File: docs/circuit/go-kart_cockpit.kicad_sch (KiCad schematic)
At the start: 41 parts, among them P1 Power, Q1 TIP120, SW1 SW_MEC_5E, X1 Taster rechts (male), X10 Bluetooth-Modul, X11 Display (male), X12 PD7, X13 SDA, X14 PG4, X15 AVR-ISP-10, X16 Taster links (male), X17 Start/Stop/Rückwärts, X2 5V, X3 GND, X4 24V Hupe, X5 SCL, X6 CS, X7 PB6, X8 J5, X9 J3

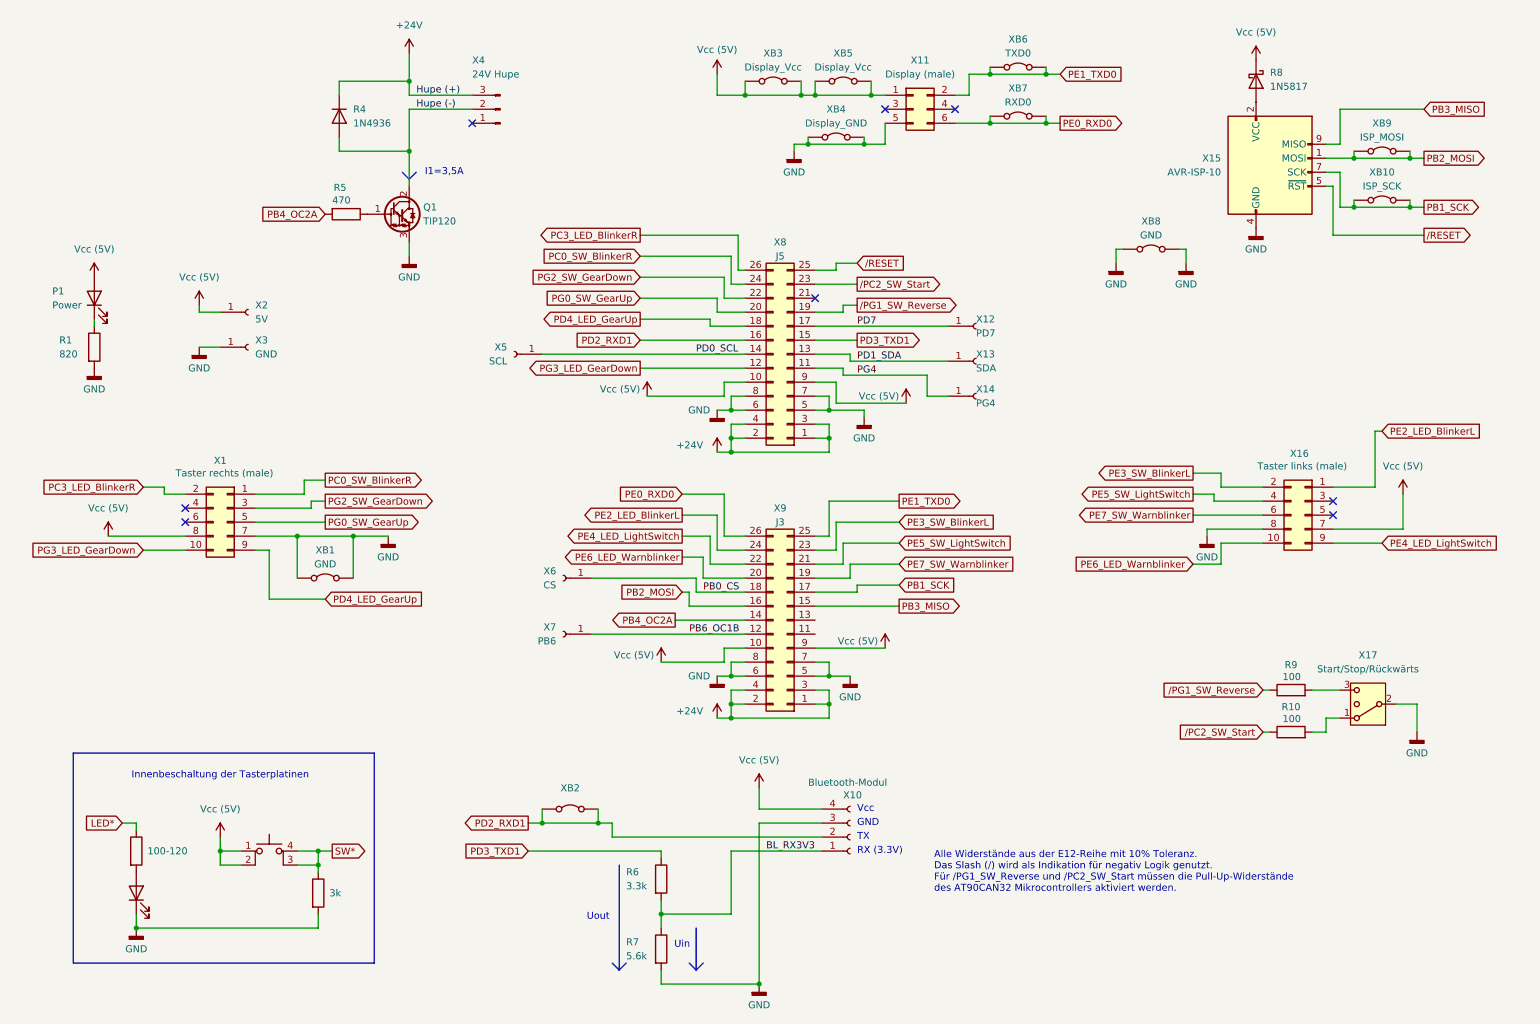
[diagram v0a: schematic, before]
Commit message: feat(PCB): add pull down resistor in preperation for FET
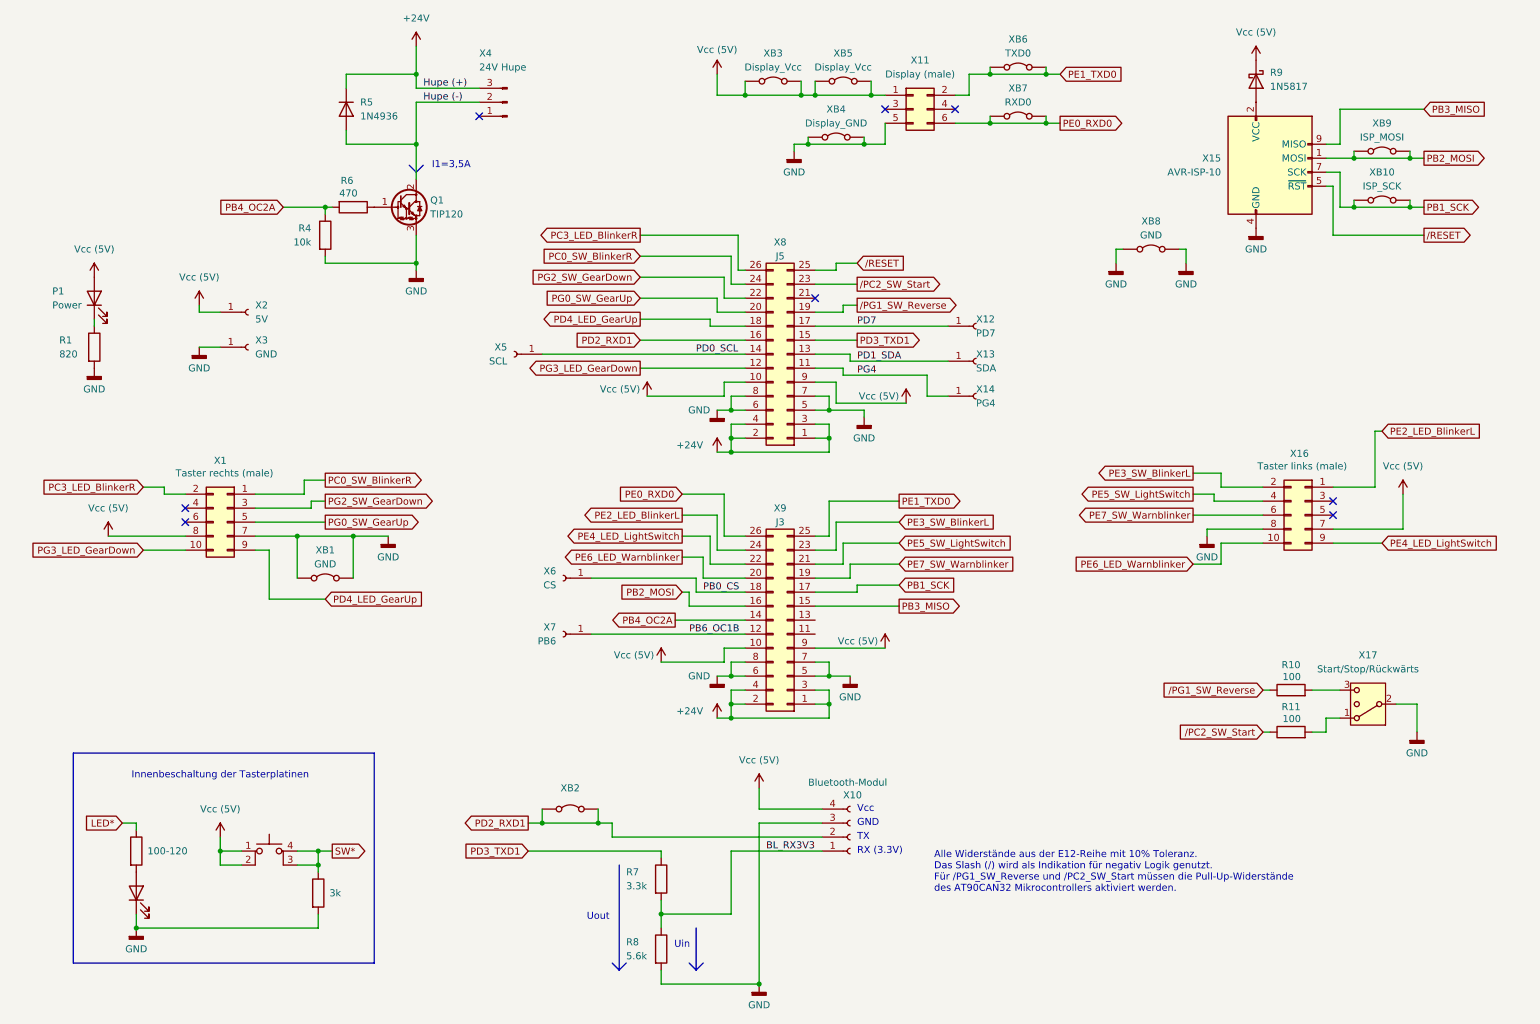
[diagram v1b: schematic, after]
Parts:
- added R4: 10k, Resistor_THT:R_Axial_DIN0207_L6.3mm_D2.5mm_P7.62mm_Horizontal, symbol Device:R
- renumbered R9 to R10, R10 to R11, R4 to R5, R5 to R6, R6 to R7, R7 to R8, R8 to R9
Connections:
- net GND: now also R4.2
- net PB4_OC2A: now also R4.1
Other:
- moved on the sheet: Q1, R5, R6, X4

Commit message: feat(PCB): improve connectors and position
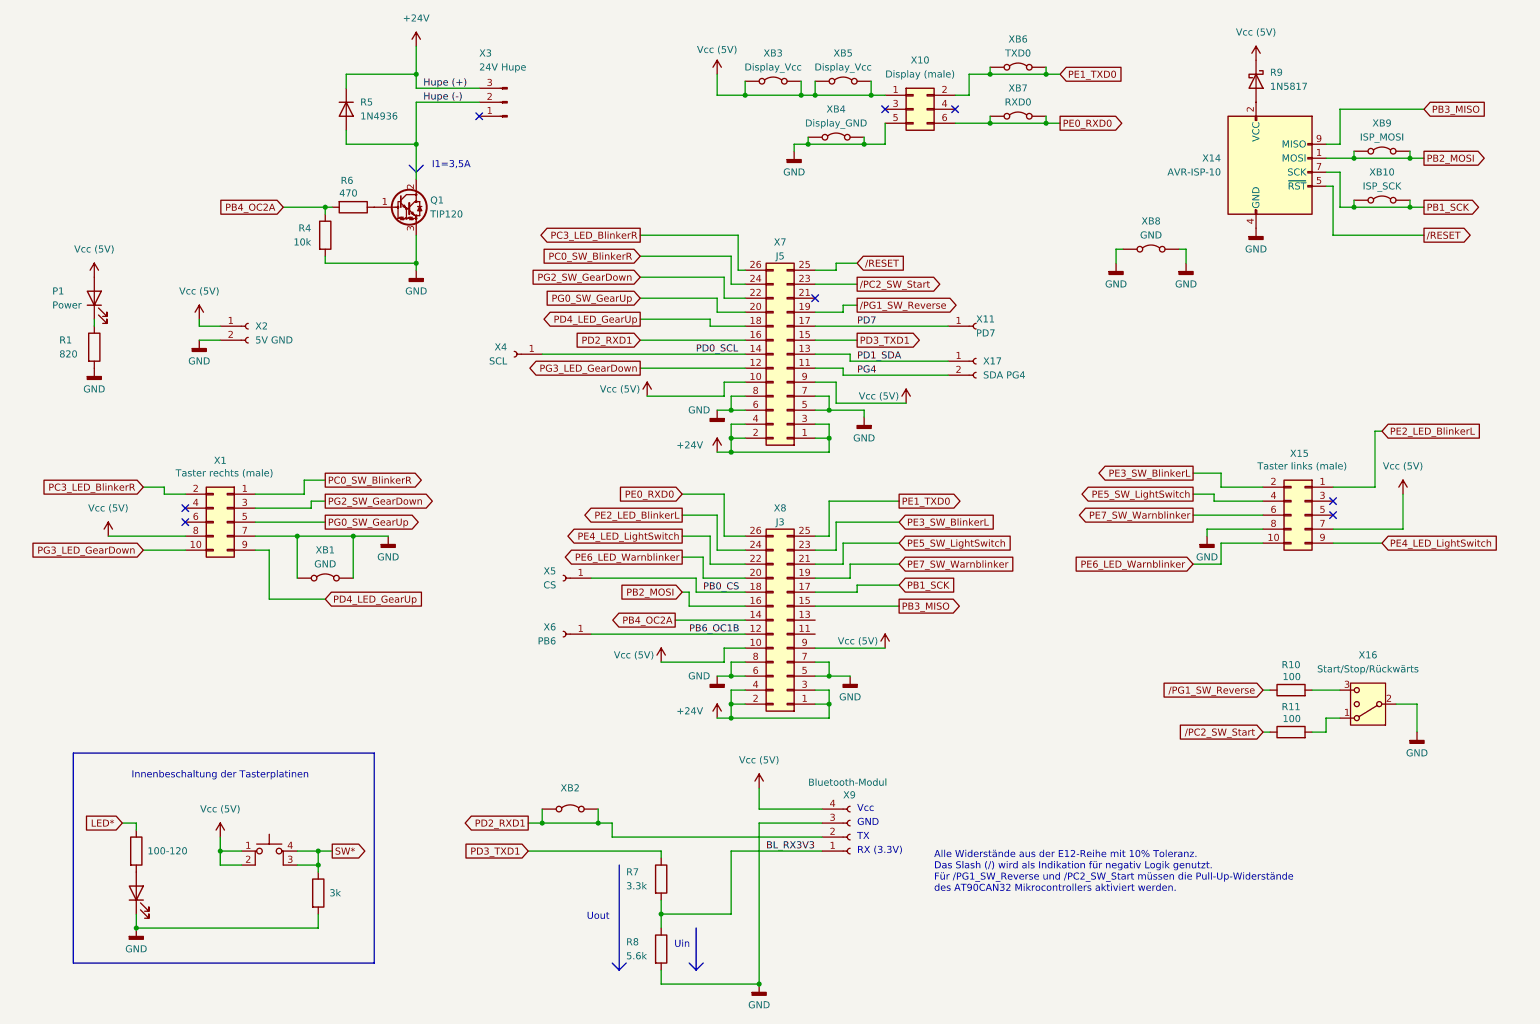
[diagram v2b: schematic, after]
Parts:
- removed X13: SDA, Connector_PinSocket_2.54mm:PinSocket_1x01_P2.54mm_Vertical, symbol Connector:Conn_01x01_Socket
- removed X14: PG4, Connector_PinSocket_2.54mm:PinSocket_1x01_P2.54mm_Vertical, symbol Connector:Conn_01x01_Socket
- removed X2: 5V, Connector_PinSocket_2.54mm:PinSocket_1x01_P2.54mm_Vertical, symbol Connector:Conn_01x01_Socket
- removed X3: GND, Connector_PinSocket_2.54mm:PinSocket_1x01_P2.54mm_Vertical, symbol Connector:Conn_01x01_Socket
- added X17: SDA PG4, Connector_PinSocket_2.54mm:PinSocket_1x02_P2.54mm_Vertical, symbol Connector:Conn_01x02_Socket
- added X2: 5V GND, Connector_PinSocket_2.54mm:PinSocket_1x02_P2.54mm_Vertical, symbol Connector:Conn_01x02_Socket
- renumbered X11 to X10, X12 to X11, X15 to X14, X16 to X15, X17 to X16, X4 to X3, X5 to X4, X6 to X5, X7 to X6, X8 to X7, X9 to X8, X10 to X9
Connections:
- net GND: now also X2.2 (Pin_2)
- net PD1_SDA: now also X17.1 (Pin_1)
- net PG4: now also X17.2 (Pin_2)
- net Vcc (5V): now also X2.1 (Pin_1)

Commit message: feat(PCB): replace TIP120 with MOSFET
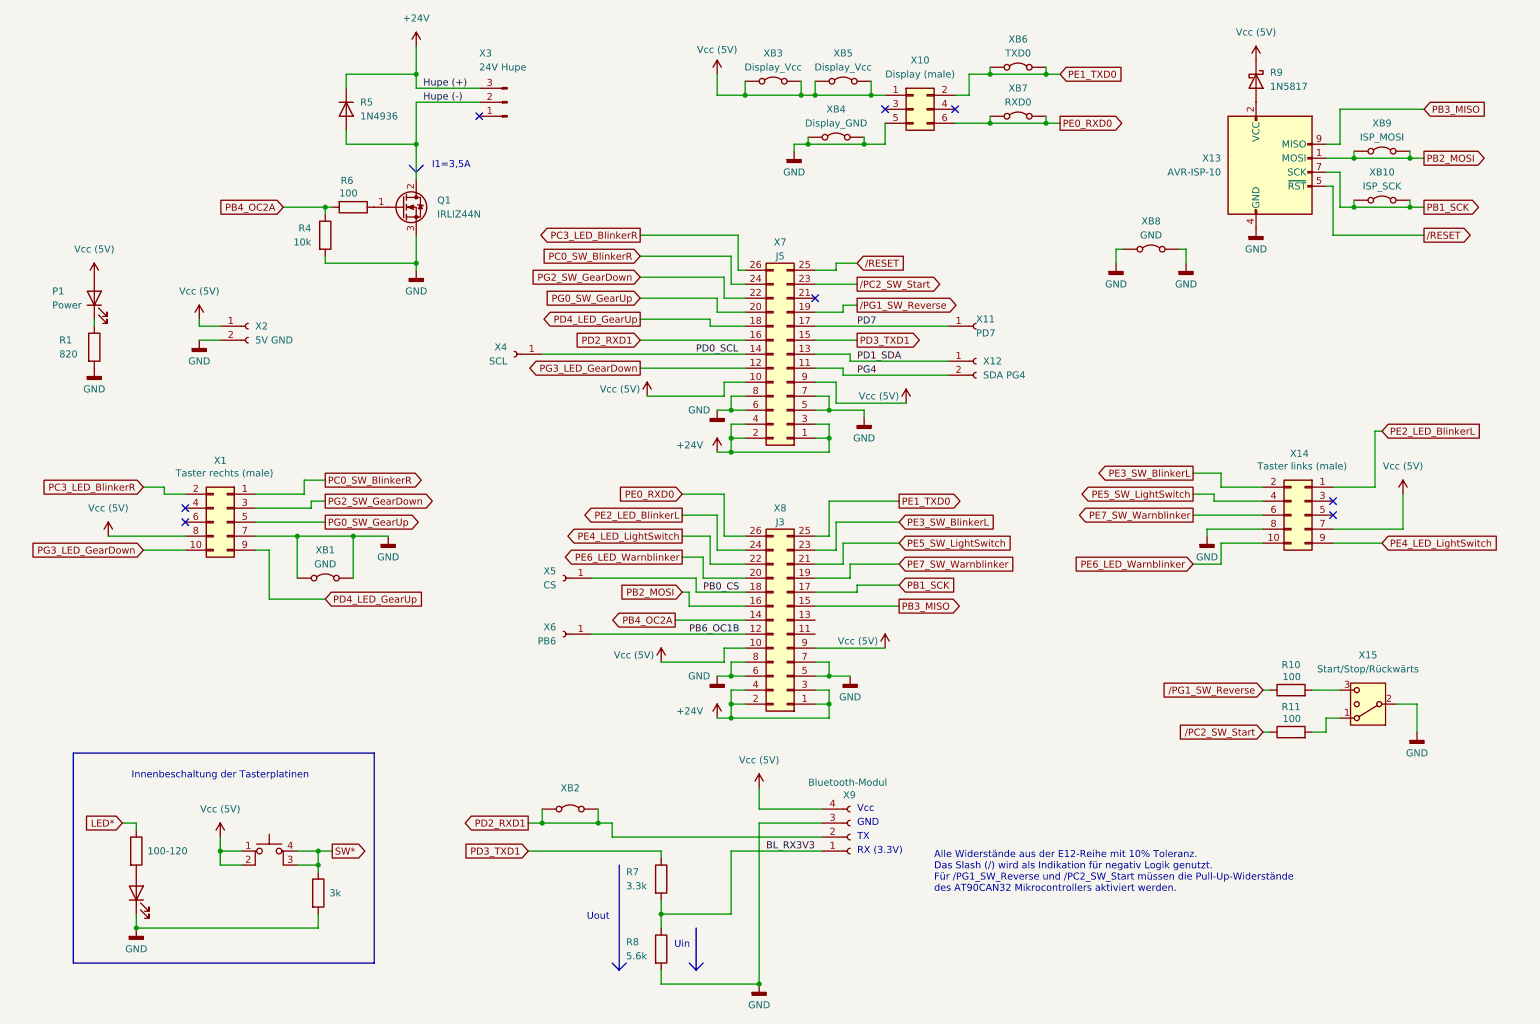
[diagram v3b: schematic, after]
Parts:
- removed Q1: TIP120, Library:TO-220-3_Horizontal_TabDown_no_hole, symbol Transistor_BJT:TIP120
- added Q1: IRLIZ44N, Library:TO-220-3_Horizontal_TabDown_no_hole, symbol Transistor_FET:IRLIZ44N
- R6: value 470 -> 100
- renumbered X17 to X12, X14 to X13, X15 to X14, X16 to X15
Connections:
- net GND: now also Q1.3 (S)
- net Hupe (-): now also Q1.2 (D)
- net at R6.1: now also Q1.1 (G)
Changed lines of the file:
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@@
 			)
 		)
-		(property "Value" "470"
+		(property "Value" "100"
 			(at 71.12 48.26 90)
 			(effects
@@
 	)
 	(symbol
-		(lib_id "Transistor_BJT:TIP120")
-		(at 82.55 50.8 0)
-		(unit 1)
-		(exclude_from_sim no)
-		(in_bom yes)
-		(on_board yes)
-		(dnp no)
-		(property "Reference" "Q1"
-			(at 87.63 49.53 0)
-			(effects
-				(font
-					(size 1.27 1.27)
-				)
-				(justify left)
-			)
-		)
-		(property "Value" "TIP120"
-			(at 87.63 52.07 0)
-			(effects
-				(font
-					(size 1.27 1.27)
-				)
-				(justify left)
-			)
-		)
-		(property "Footprint" "Library:TO-220-3_Horizontal_TabDown_no_hole"
-			(at 87.63 52.705 0)
-			(effects
-				(font
-					(size 1.27 1.27)
-					(italic yes)
-				)
-				(justify left)
-				(hide yes)
-			)
-		)
-		(property "Datasheet" "https://www.onsemi.com/pub/Collateral/TIP120-D.PDF"
-			(at 82.55 50.8 0)
-			(effects
-				(font
-					(size 1.27 1.27)
-				)
-				(justify left)
-				(hide yes)
-			)
-		)
-		(property "Description" "5A Ic, 60V Vce, Silicon Darlington Power NPN Transistor, TO-220"
-			(at 82.55 50.8 0)
-			(effects
-				(font
-					(size 1.27 1.27)
-				)
-				(hide yes)
-			)
-		)
-		(pin "3"
-		)
-		(pin "2"
-		)
-		(pin "1"
-		)
-		(instances
-			(project ""
-				(path "/e785e5e4-6da9-4e03-ba54-b62675208098"
-					(reference "Q1")
-					(unit 1)
-				)
-			)
-		)
-	)
-	(symbol
 		(lib_id "Jumper:Jumper_2_Bridged")
 		(at 194.31 25.4 0)
@@
 		(dnp no)
 		(fields_autoplaced yes)
-		(property "Reference" "X14"
+		(property "Reference" "X13"
 			(at 231.14 41.9099 0)
 			(effects
@@
 			(project ""
 				(path "/e785e5e4-6da9-4e03-ba54-b62675208098"
-					(reference "X14")
+					(reference "X13")
 					(unit 1)
 				)
@@
 		(dnp no)
 		(fields_autoplaced yes)
-		(property "Reference" "X17"
+		(property "Reference" "X12"
 			(at 187.96 78.7399 0)
 			(effects
@@
 			(project "go-kart_cockpit"
 				(path "/e785e5e4-6da9-4e03-ba54-b62675208098"
-					(reference "X17")
+					(reference "X12")
 					(unit 1)
 				)
@@
 	)
 	(symbol
+		(lib_id "Transistor_FET:IRLIZ44N")
+		(at 82.55 50.8 0)
+		(unit 1)
+		(exclude_from_sim no)
+		(in_bom yes)
+		(on_board yes)
+		(dnp no)
+		(fields_autoplaced yes)
+		(property "Reference" "Q1"
+			(at 88.9 49.5299 0)
+			(effects
+				(font
+					(size 1.27 1.27)
+				)
+				(justify left)
+			)
+		)
+		(property "Value" "IRLIZ44N"
+			(at 88.9 52.0699 0)
+			(effects
+				(font
+					(size 1.27 1.27)
+				)
+				(justify left)
+			)
+		)
+		(property "Footprint" "Library:TO-220-3_Horizontal_TabDown_no_hole"
+			(at 87.63 52.705 0)
+			(effects
+				(font
+					(size 1.27 1.27)
+					(italic yes)
+				)
+				(justify left)
+				(hide yes)
+			)
+		)
+		(property "Datasheet" "http://www.irf.com/product-info/datasheets/data/irliz44n.pdf"
+			(at 87.63 54.61 0)
+			(effects
+				(font
+					(size 1.27 1.27)
+				)
+				(justify left)
+				(hide yes)
+			)
+		)
+		(property "Description" "30A Id, 55V Vds, 22mOhm Rds, N-Channel HEXFET Power MOSFET, TO-220AB"
+			(at 82.55 50.8 0)
+			(effects
+				(font
+					(size 1.27 1.27)
+				)
+				(hide yes)
+			)
+		)
+		(pin "3"
+		)
+		(pin "2"
+		)
+		(pin "1"
+		)
+		(instances
+			(project ""
+				(path "/e785e5e4-6da9-4e03-ba54-b62675208098"
+					(reference "Q1")
+					(unit 1)
+				)
+			)
+		)
+	)
+	(symbol
 		(lib_id "power:VCC")
 		(at 173.99 86.36 0)
@@
 		(dnp no)
 		(fields_autoplaced yes)
-		(property "Reference" "X16"
+		(property "Reference" "X15"
 			(at 257.81 132.08 0)
 			(effects
@@
 			(project "go-kart_cockpit"
 				(path "/e785e5e4-6da9-4e03-ba54-b62675208098"
-					(reference "X16")
+					(reference "X15")
 					(unit 1)
 				)
@@
 		(on_board yes)
 		(dnp no)
-		(property "Reference" "X15"
+		(property "Reference" "X14"
 			(at 245.364 95.504 0)
 			(effects
@@
 			(project ""
 				(path "/e785e5e4-6da9-4e03-ba54-b62675208098"
-					(reference "X15")
+					(reference "X14")
 					(unit 1)
 				)
